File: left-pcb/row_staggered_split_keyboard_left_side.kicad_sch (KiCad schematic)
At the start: 3 parts, among them U1 SN74LVC1T45DBV

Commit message: Updating schematic with different size keys
Also updated LED data wiring to correspond with PCB layout
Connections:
- net +3V3: now also A1.22 (3V); no longer A1.18 (3V)
- net +5V: now also A1.25 (RAW); no longer A1.15 (RAW)
- net COL5: now also A1.19 (A1); no longer A1.21 (A1)
- net COL6: now also A1.18 (A0); no longer A1.22 (A0)
- net COL7: now also A1.17 (CLK); no longer A1.23 (CLK)
- net GND: now also A1.24 (G); no longer A1.16 (G)
- net PS2_CLK: now also A1.16 (MI); no longer A1.24 (MI)
- net PS2_DATA: now also A1.15 (MO); no longer A1.25 (MO)
- net at A1.14 (10): now also U1.4 (B)
- net at A1.26 (D-): no longer U1.4 (B)
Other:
- sheet R1C1: file switch_with_LED.kicad_sch -> switch_with_LED_1U.kicad_sch
- sheet R1C2: file switch_with_LED.kicad_sch -> switch_with_LED_1U.kicad_sch
- sheet R1C3: file switch_with_LED.kicad_sch -> switch_with_LED_1U.kicad_sch
- sheet R1C4: file switch_with_LED.kicad_sch -> switch_with_LED_1U.kicad_sch
- sheet R1C5: file switch_with_LED.kicad_sch -> switch_with_LED_1U.kicad_sch
- sheet R1C6: file switch_with_LED.kicad_sch -> switch_with_LED_1U.kicad_sch
- sheet R1C7: file switch_with_LED.kicad_sch -> switch_with_LED_1U.kicad_sch
- sheet R2C1: file switch_with_LED.kicad_sch -> switch_with_LED_1U.kicad_sch
- sheet R2C2: file switch_with_LED.kicad_sch -> switch_with_LED_1U.kicad_sch
- sheet R2C3: file switch_with_LED.kicad_sch -> switch_with_LED_1U.kicad_sch
- sheet R2C4: file switch_with_LED.kicad_sch -> switch_with_LED_1U.kicad_sch
- sheet R2C5: file switch_with_LED.kicad_sch -> switch_with_LED_1U.kicad_sch
- sheet R2C6: file switch_with_LED.kicad_sch -> switch_with_LED_1U.kicad_sch
- sheet R2C7: file switch_with_LED.kicad_sch -> switch_with_LED_1U.kicad_sch
- sheet R3C1: file switch_with_LED.kicad_sch -> switch_with_LED_1U.kicad_sch
- sheet R3C2: file switch_with_LED.kicad_sch -> switch_with_LED_1U.kicad_sch
- sheet R3C3: file switch_with_LED.kicad_sch -> switch_with_LED_1U.kicad_sch
- sheet R3C4: file switch_with_LED.kicad_sch -> switch_with_LED_1U.kicad_sch
- sheet R3C5: file switch_with_LED.kicad_sch -> switch_with_LED_1U.kicad_sch
- sheet R3C6: file switch_with_LED.kicad_sch -> switch_with_LED_1U.kicad_sch
- sheet R3C7: file switch_with_LED.kicad_sch -> switch_with_LED_1U.kicad_sch
- sheet R4C1: file switch_with_LED.kicad_sch -> switch_with_LED_1U5.kicad_sch
- sheet R4C2: file switch_with_LED.kicad_sch -> switch_with_LED_1U.kicad_sch
- sheet R4C3: file switch_with_LED.kicad_sch -> switch_with_LED_1U.kicad_sch
- sheet R4C4: file switch_with_LED.kicad_sch -> switch_with_LED_1U.kicad_sch
- sheet R4C5: file switch_with_LED.kicad_sch -> switch_with_LED_1U.kicad_sch
- sheet R4C6: file switch_with_LED.kicad_sch -> switch_with_LED_1U.kicad_sch
- sheet R4C7: file switch_with_LED.kicad_sch -> switch_with_LED_1U.kicad_sch
- sheet R5C1: file switch_with_LED.kicad_sch -> switch_with_LED_1U75.kicad_sch
- sheet R5C2: file switch_with_LED.kicad_sch -> switch_with_LED_1U.kicad_sch
- sheet R5C3: file switch_with_LED.kicad_sch -> switch_with_LED_1U.kicad_sch
- sheet R5C4: file switch_with_LED.kicad_sch -> switch_with_LED_1U.kicad_sch
- sheet R5C5: file switch_with_LED.kicad_sch -> switch_with_LED_1U.kicad_sch
- sheet R5C6: file switch_with_LED.kicad_sch -> switch_with_LED_1U.kicad_sch
- sheet R5C7: file switch_with_LED.kicad_sch -> switch_with_LED_1U.kicad_sch
- sheet R6C1: file switch_with_LED.kicad_sch -> switch_with_LED_2U.kicad_sch
- sheet R6C2: file switch_with_LED.kicad_sch -> switch_with_LED_1U.kicad_sch
- sheet R6C3: file switch_with_LED.kicad_sch -> switch_with_LED_1U.kicad_sch
- sheet R6C4: file switch_with_LED.kicad_sch -> switch_with_LED_1U.kicad_sch
- sheet R6C5: file switch_with_LED.kicad_sch -> switch_with_LED_1U.kicad_sch
- sheet R6C6: file switch_with_LED.kicad_sch -> switch_with_LED_1U.kicad_sch
- sheet R6C7: file switch_with_LED.kicad_sch -> switch_with_LED_1U.kicad_sch
- sheet R7C1: file switch_with_LED.kicad_sch -> switch_with_LED_1U25.kicad_sch
- sheet R7C2: file switch_with_LED.kicad_sch -> switch_with_LED_1U25.kicad_sch
- sheet R7C3: file switch_with_LED.kicad_sch -> switch_with_LED_1U25.kicad_sch
- sheet R7C4: file switch_with_LED.kicad_sch -> switch_with_LED_2U25.kicad_sch
- sheet R7C5: file switch_with_LED.kicad_sch -> switch_with_LED_1U.kicad_sch
- sheet R7C6: file switch_with_LED.kicad_sch -> switch_with_LED_1U.kicad_sch
- sheet R7C7: file switch_with_LED.kicad_sch -> switch_with_LED_1U.kicad_sch
- note added: "1"
- note added: "2"
- note added: "3"
- note added: "4"
- note added: "5"
- note added: "6"
- note added: "A"
- note added: "ALT"
- note added: "B"
- note added: "BACKTICK"
- note added: "C"
- note added: "CAPS"
- note added: "CTL"
- note added: "D"
- note added: "E"
- note added: "ESC"
- note added: "F"
- note added: "F1"
- note added: "F2"
- note added: "F3"
- note added: "F4"
- note added: "F5"
- note added: "F6"
- note added: "F?"
- note added: "G"
- note added: "M1"
- note added: "M2"
- note added: "M3"
- note added: "M4"
- note added: "M5"
- note added: "M6"
- note added: "META"
- note added: "Q"
- note added: "R"
- note added: "S"
- note added: "SHIFT"
- note added: "SPACE"
- note added: "T"
- note added: "TAB"
- note added: "V"
- note added: "W"
- note added: "X"
- note added: "Z"

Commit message: Next revision of PCB
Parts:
- removed A2: SK8707-01, Connector_PinHeader_1.27mm:PinHeader_1x08_P1.27mm_Vertical, symbol SW-Sprintek:SK8707-1
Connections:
- net COL1: now also A1.7 (3); no longer A1.11 (7)
- net COL2: now also A1.8 (4); no longer A1.12 (8)
- net COL3: now also A1.9 (5); no longer A1.13 (9)
- net COL4: now also A1.10 (6); no longer A1.20 (A2)
- net COL5: now also A1.11 (7); no longer A1.19 (A1)
- net COL6: now also A1.12 (8); no longer A1.18 (A0)
- net COL7: now also A1.13 (9); no longer A1.17 (CLK)
- net ROW4: now also A1.21 (A3); no longer A1.7 (3)
- net ROW5: now also A1.20 (A2); no longer A1.8 (4)
- net ROW6: now also A1.19 (A1); no longer A1.9 (5)
- net ROW7: now also A1.18 (A0); no longer A1.10 (6)
- net PS2_CLK: no longer names the net of A1.16 (MI)
- net PS2_DATA: no longer names the net of A1.15 (MO)
- no-connect marks 9 -> 7
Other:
- note removed: "Maybe have trackpoint on own KB2040?"
- note removed: "PS2_DATA = GPIO19 PS2_CLK = GPIO20"

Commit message: Initial modifications to reduce fab cost and add caps
Removing 1 row and column of keys, and majorly changing layout

Routing still in progress
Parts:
- added C1, C4: 1uF, Capacitor_SMD:C_1206_3216Metric_Pad1.33x1.80mm_HandSolder, symbol Device:C_Small
- added C2, C3: 100nF, Capacitor_SMD:C_1206_3216Metric_Pad1.33x1.80mm_HandSolder, symbol Device:C_Small
- added H1, H2, H3, H4: MountingHole, MountingHole:MountingHole_4.3mm_M4, symbol Mechanical:MountingHole
- A1: footprint Package_DIP:DIP-26_W15.24mm_Socket -> SW-Adafruit:KB2024_Socketed
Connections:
- net +3V3: now also C1.1, C2.1
- net +5V: now also C3.1, C4.1
- net GND: now also C1.2, C2.2, C3.2, C4.2
- net COL7: no longer names the net of A1.13 (9)
- net ROW7: no longer names the net of A1.18 (A0)
- no-connect marks 7 -> 9
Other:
- removed sheet R1C7
- removed sheet R2C7
- removed sheet R3C7
- removed sheet R4C7
- removed sheet R5C7
- removed sheet R6C6
- removed sheet R6C7
- removed sheet R7C1
- removed sheet R7C2
- removed sheet R7C3
- removed sheet R7C4
- removed sheet R7C5
- removed sheet R7C6
- removed sheet R7C7
- sheet R3C1: file switch_with_LED_1U.kicad_sch -> switch_with_LED_1U5.kicad_sch
- sheet R4C1: file switch_with_LED_1U5.kicad_sch -> switch_with_LED_1U75.kicad_sch
- sheet R5C1: file switch_with_LED_1U75.kicad_sch -> switch_with_LED_2U.kicad_sch
- sheet R6C1: file switch_with_LED_2U.kicad_sch -> switch_with_LED_1U25.kicad_sch
- sheet R6C2: file switch_with_LED_1U.kicad_sch -> switch_with_LED_1U25.kicad_sch
- sheet R6C3: file switch_with_LED_1U.kicad_sch -> switch_with_LED_1U25.kicad_sch
- sheet R6C4: file switch_with_LED_1U.kicad_sch -> switch_with_LED_2U25.kicad_sch
- note added: "FN"
- note removed: "F5"
- note removed: "F6"
- note removed: "F?"
- note removed: "M1"
- note removed: "M2"
- note removed: "M3"
- note removed: "M4"
- note removed: "M5"
- note removed: "M6"
- note removed: "TODO: Need to add caps for supply filtering on level shifter"
- moved on the sheet: A1, U1

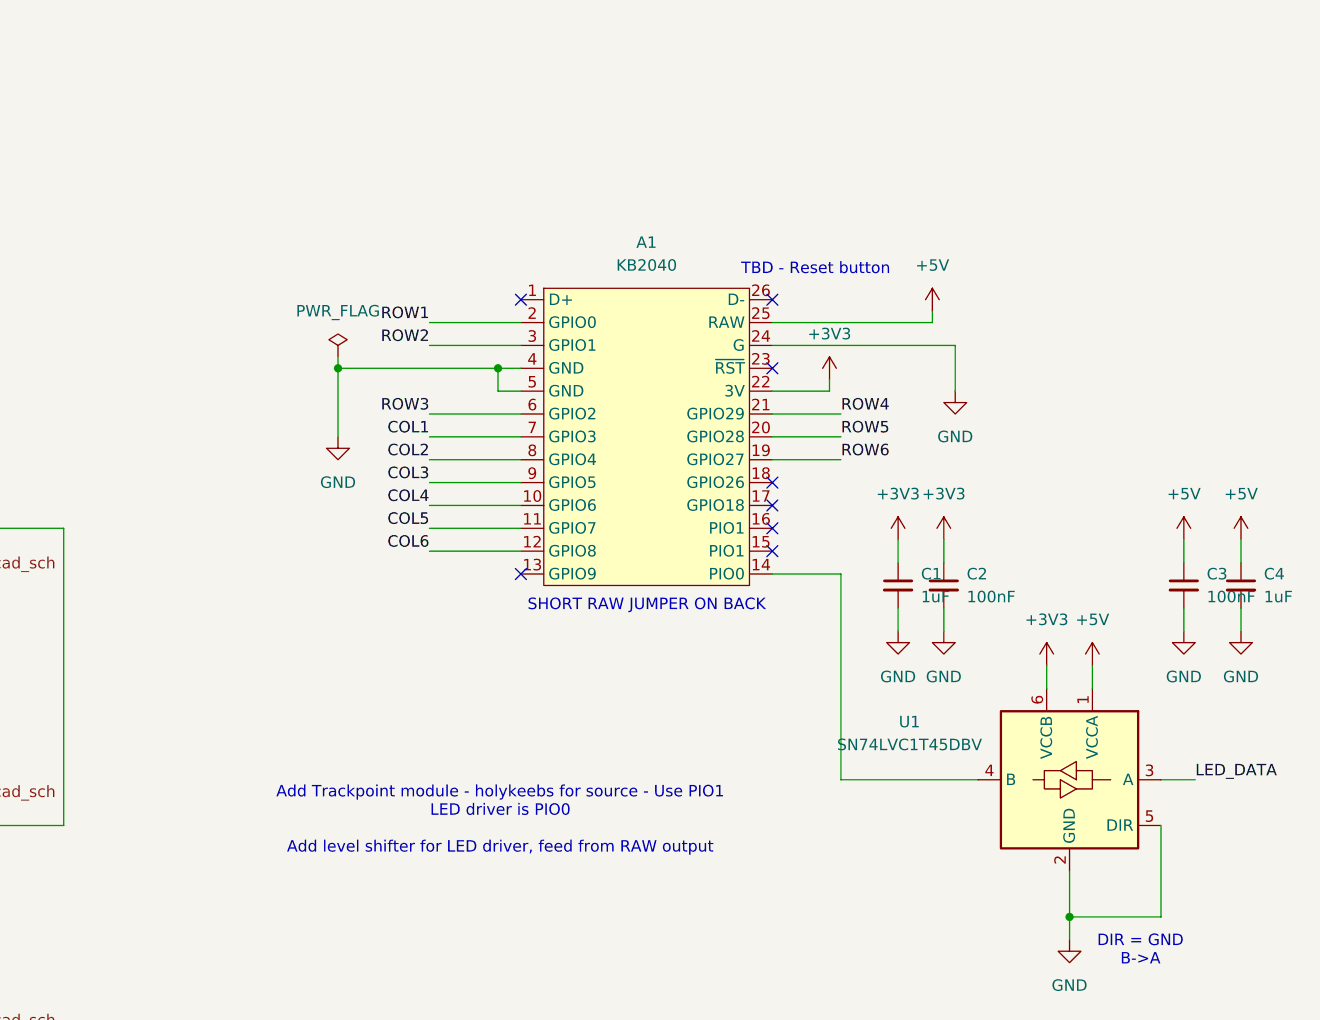
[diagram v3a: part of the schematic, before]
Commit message: Caps, shrunk board, added mounting holes
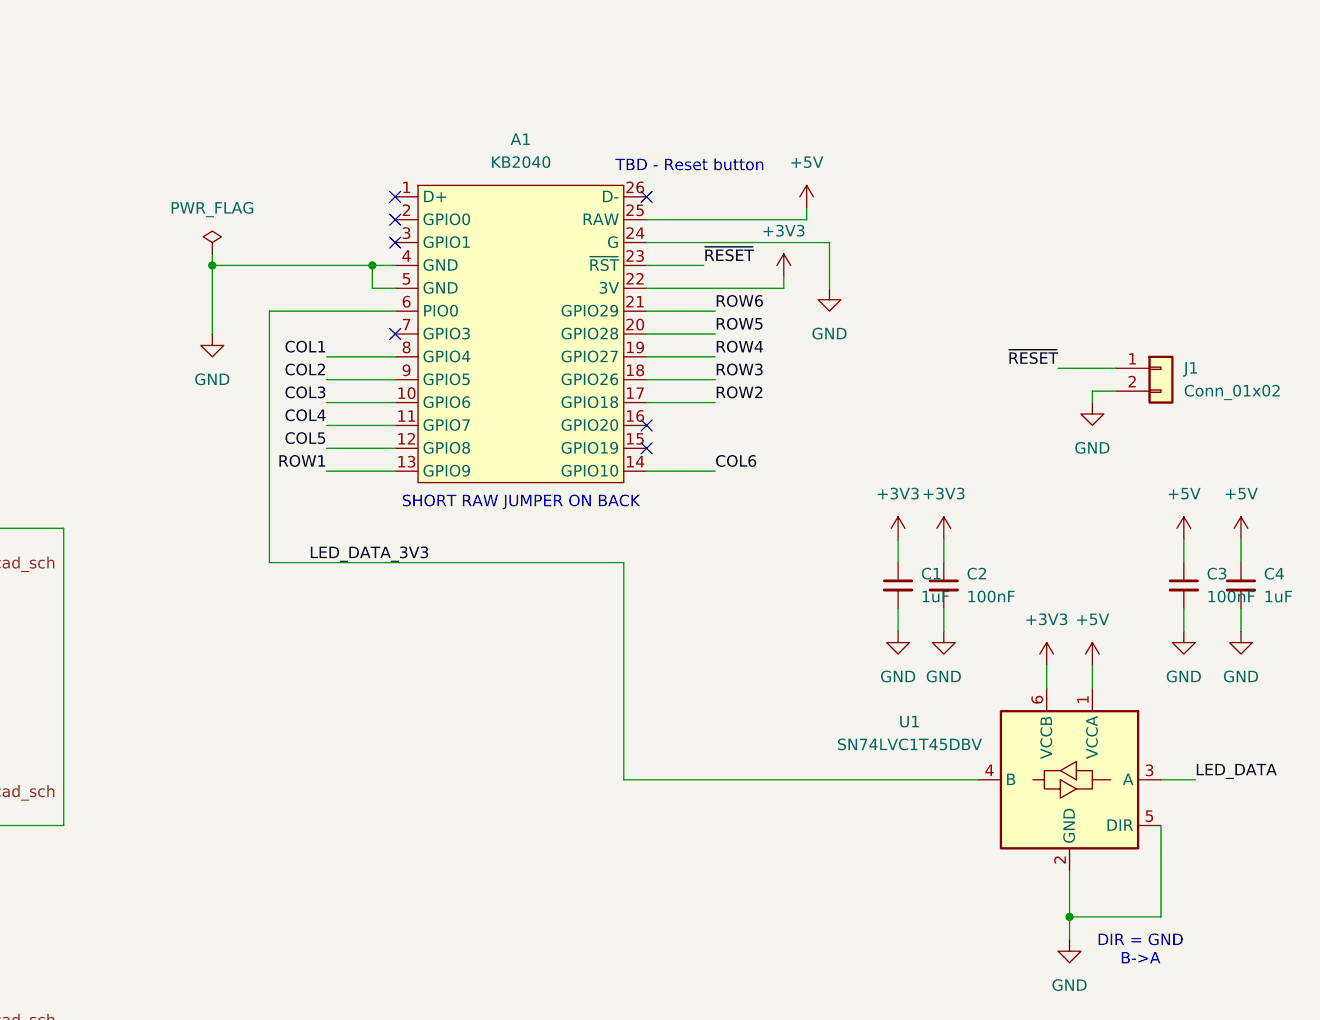
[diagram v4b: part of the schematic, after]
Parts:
- added J1: Conn_01x02, Connector_PinSocket_2.54mm:PinSocket_1x02_P2.54mm_Vertical, symbol Connector_Generic:Conn_01x02
- C1, C2, C3, C4: footprint Capacitor_SMD:C_1206_3216Metric_Pad1.33x1.80mm_HandSolder -> Capacitor_SMD:C_0805_2012Metric_Pad1.18x1.45mm_HandSolder
- H1, H2, H3, H4: footprint MountingHole:MountingHole_4.3mm_M4 -> MountingHole:MountingHole_3.2mm_M3_ISO14580
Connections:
- net COL1: now also A1.8 (4); no longer A1.7 (3)
- net COL2: now also A1.9 (5); no longer A1.8 (4)
- net COL3: now also A1.10 (6); no longer A1.9 (5)
- net COL4: now also A1.11 (7); no longer A1.10 (6)
- net COL5: now also A1.12 (8); no longer A1.11 (7)
- net COL6: now also A1.14 (10); no longer A1.12 (8)
- net GND: now also J1.2 (Pin_2)
- net ROW1: now also A1.13 (9); no longer A1.2 (TX)
- net ROW2: now also A1.17 (CLK); no longer A1.3 (RX)
- net ROW3: now also A1.18 (A0); no longer A1.6 (2)
- net ROW4: now also A1.19 (A1); no longer A1.21 (A3)
- net ROW6: now also A1.21 (A3); no longer A1.19 (A1)
- net LED_DATA_3V3: now reaches U1.4 (B)
- net LED_DATA_3V3: now also A1.6 (2); no longer A1.14 (10)
- net ~{RESET}: now reaches A1.23 (~{RST})
- net ~{RESET}: now also J1.1 (Pin_1)
- no-connect marks 9 -> 8
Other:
- note removed: "Add Trackpoint module - holykeebs for source - Use PIO1 LED driver is PIO0 Add level shifter for LED driver, feed from RAW output"
- moved on the sheet: A1

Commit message: Added extra column to left hand keyboard
Matching size to right hand side.
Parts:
- H1, H2, H3, H4: value MountingHole -> M3
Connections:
- net COL0: now reaches A1.7 (3)
- no-connect marks 8 -> 7
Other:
- added sheet R1C0 (switch_with_LED_1U.kicad_sch)
- added sheet R2C0 (switch_with_LED_1U.kicad_sch)
- added sheet R3C0 (switch_with_LED_1U.kicad_sch)
- added sheet R4C0 (switch_with_LED_1U.kicad_sch)
- added sheet R5C0 (switch_with_LED_1U.kicad_sch)
- added sheet R6C0 (switch_with_LED_1U.kicad_sch)
- note added: "F10"
- note added: "F5"
- note added: "F6"
- note added: "F7"
- note added: "F8"
- note added: "F9"
- moved on the sheet: A1, C1, C2, C3, C4, H1, H2, H3, H4, J1, U1

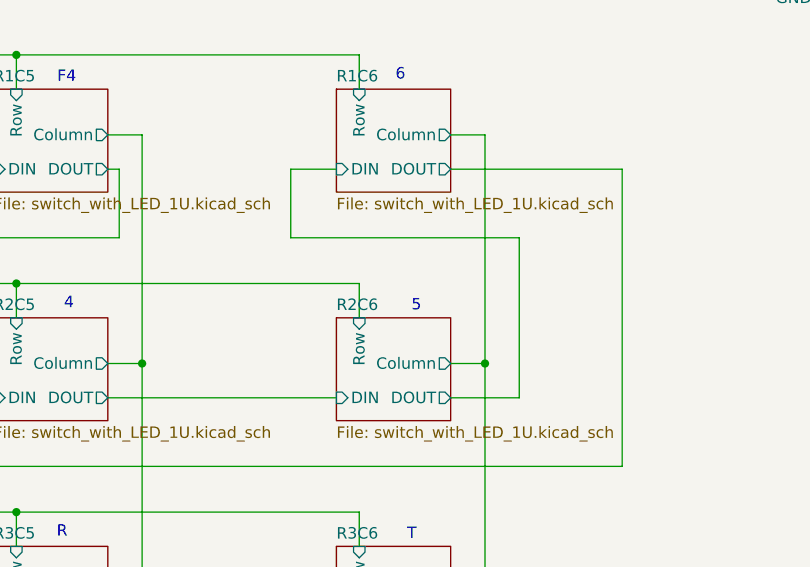
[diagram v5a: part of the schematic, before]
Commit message: reworking LED data lines to eliminate ground plane disconnections
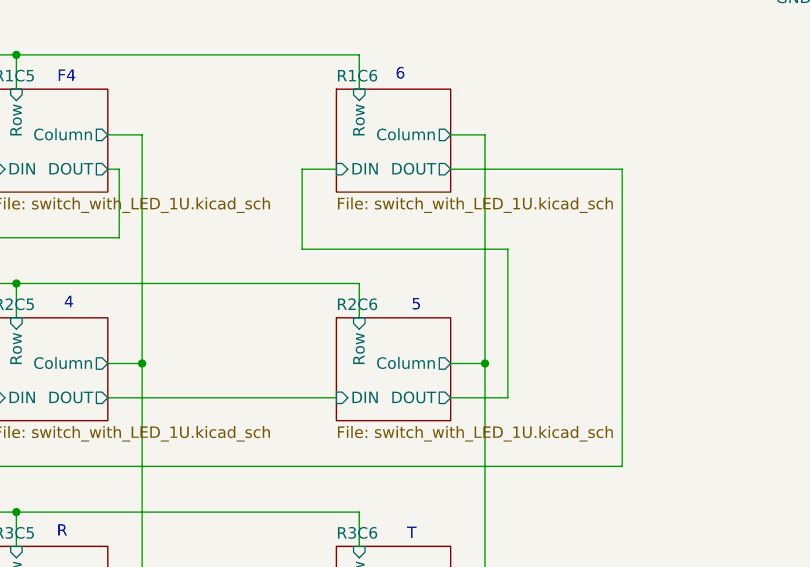
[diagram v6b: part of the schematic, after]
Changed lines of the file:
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@@
+	(wire
+		(pts
+			(xy 276.86 72.39) (xy 280.67 72.39)
+		)
+		(stroke
+			(width 0)
+			(type default)
+		)
+	)
 	(wire
 		(pts
@@
 	(wire
 		(pts
-			(xy 293.37 97.79) (xy 300.99 97.79)
-		)
-		(stroke
-			(width 0)
-			(type default)
-		)
-	)
-	(wire
-		(pts
 			(xy 140.97 170.18) (xy 144.78 170.18)
 		)
@@
 	(wire
 		(pts
+			(xy 293.37 97.79) (xy 299.72 97.79)
+		)
+		(stroke
+			(width 0)
+			(type default)
+		)
+	)
+	(wire
+		(pts
 			(xy 64.77 97.79) (xy 90.17 97.79)
 		)
@@
 	(wire
 		(pts
-			(xy 275.59 80.01) (xy 275.59 72.39)
-		)
-		(stroke
-			(width 0)
-			(type default)
-		)
-	)
-	(wire
-		(pts
 			(xy 168.91 59.69) (xy 168.91 63.5)
 		)
@@
 	(wire
 		(pts
-			(xy 275.59 72.39) (xy 280.67 72.39)
-		)
-		(stroke
-			(width 0)
-			(type default)
-		)
-	)
-	(wire
-		(pts
 			(xy 64.77 199.39) (xy 90.17 199.39)
 		)
@@
 	(wire
 		(pts
+			(xy 299.72 81.28) (xy 276.86 81.28)
+		)
+		(stroke
+			(width 0)
+			(type default)
+		)
+	)
+	(wire
+		(pts
 			(xy 245.11 85.09) (xy 283.21 85.09)
 		)
@@
 	(wire
 		(pts
+			(xy 299.72 97.79) (xy 299.72 81.28)
+		)
+		(stroke
+			(width 0)
+			(type default)
+		)
+	)
+	(wire
+		(pts
 			(xy 245.11 135.89) (xy 245.11 139.7)
 		)
@@
 	(wire
 		(pts
-			(xy 300.99 97.79) (xy 300.99 80.01)
-		)
-		(stroke
-			(width 0)
-			(type default)
-		)
-	)
-	(wire
-		(pts
 			(xy 207.01 135.89) (xy 245.11 135.89)
 		)
@@
 	(wire
 		(pts
-			(xy 300.99 80.01) (xy 275.59 80.01)
-		)
-		(stroke
-			(width 0)
-			(type default)
-		)
-	)
-	(wire
-		(pts
 			(xy 245.11 135.89) (xy 283.21 135.89)
 		)
@@
 		)
 		(stroke
+			(width 0)
+			(type default)
+		)
+	)
+	(wire
+		(pts
+			(xy 276.86 81.28) (xy 276.86 72.39)
+		)
+		(stroke

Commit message: Silkscreen cleanup and trace cleanup in prep for PCB review posting
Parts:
- J1: now left out of the parts list
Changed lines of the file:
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@@
 		(unit 1)
 		(exclude_from_sim no)
-		(in_bom yes)
+		(in_bom no)
 		(on_board yes)
 		(dnp no)

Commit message: updating for KiCAD 10.0
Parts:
- A1, C1, C2, C3, C4, U1: now left out of the parts list
